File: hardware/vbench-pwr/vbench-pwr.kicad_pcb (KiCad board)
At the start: 2 copper layers, 150 x 136 mm, 39 parts, among them J1 COIL, J10 WAVESHARE-B, J11 WAVESHARE-C, J12 WAVESHARE-D, J2 CHARGE, J3 AUX-BANK, J4 12V-IN, J6 ISENSE, J7 PICO-L, J8 PICO-R, J9 WAVESHARE-A, Q1 IRFP4668, Q2 IRFP4668, Q3 IRFP4668, U1 UCC27524A

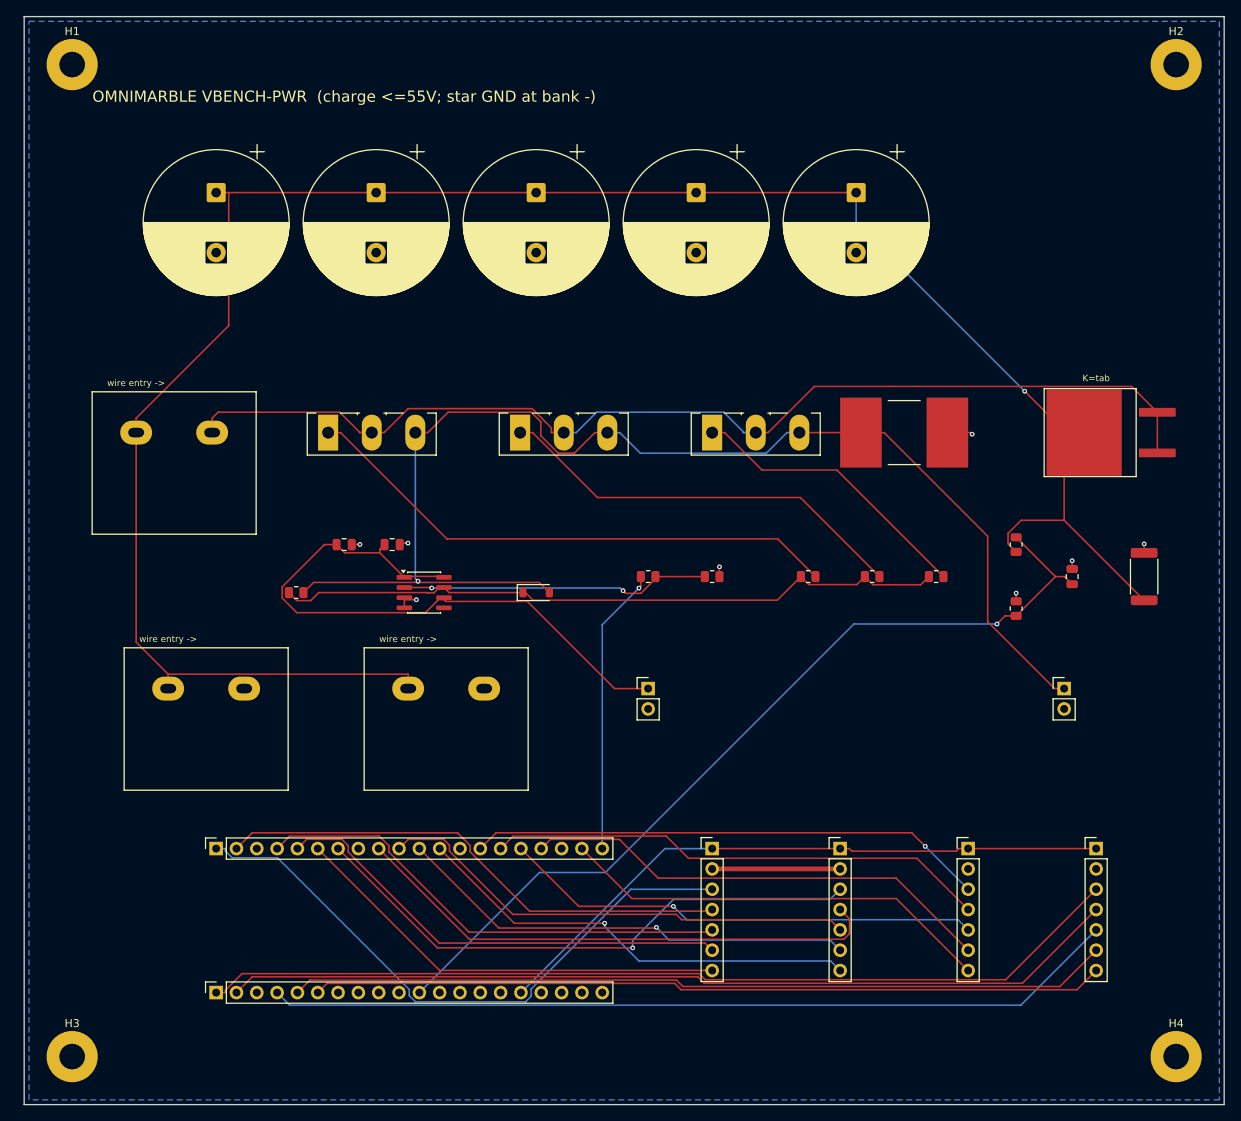
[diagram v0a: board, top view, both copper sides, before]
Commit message: vbench: harden routing to 4-layer with plane-locked inner GND planes
The 2-layer board's B.Cu GND pour fragmented into pockets wherever freerouting
routed a signal across it, and the post-hoc GND stitch was tied to one specific
route (re-routes were non-reproducible). Root cause: a 2-layer board can't hold a
solid GND plane AND route this density on the one remaining signal layer.

Fix = the driver's dedicated-plane pattern, on 4 layers:
- Stackup: F.Cu + B.Cu = signals (2 layers, freerouting completes in ~2s),
  In1 = solid GND plane, In2 = GND plane + a +3V3 pocket over the logic zone.
- plane_lock_dsn() marks In1/In2 (type power) so freerouting never routes a signal
  on them -> the GND plane is never cut, so it can't fragment.
- import drops a GND through-via at each SMD GND pad (freerouting doesn't via them
  down to the inner planes; THT GND pads reach the planes directly).
- +3V3 (all-THT: Pico 3V3 + 4 Waveshare pin-1s) connects through the In2 +3V3
  pocket by via -- no F.Cu/B.Cu routing, so no crossings.

No post-hoc stitching remains. Reproducible: repeated place->route->import runs
give the same DRC-clean board (0 unconnected / 0 parity / 1 cosmetic silk). Back to
4 Waveshare connectors (20 sensor channels). gen_fab: LAYERS_4 + inner 1oz copper.

Co-Authored-By: Claude Opus 4.8 <noreply@anthropic.com>
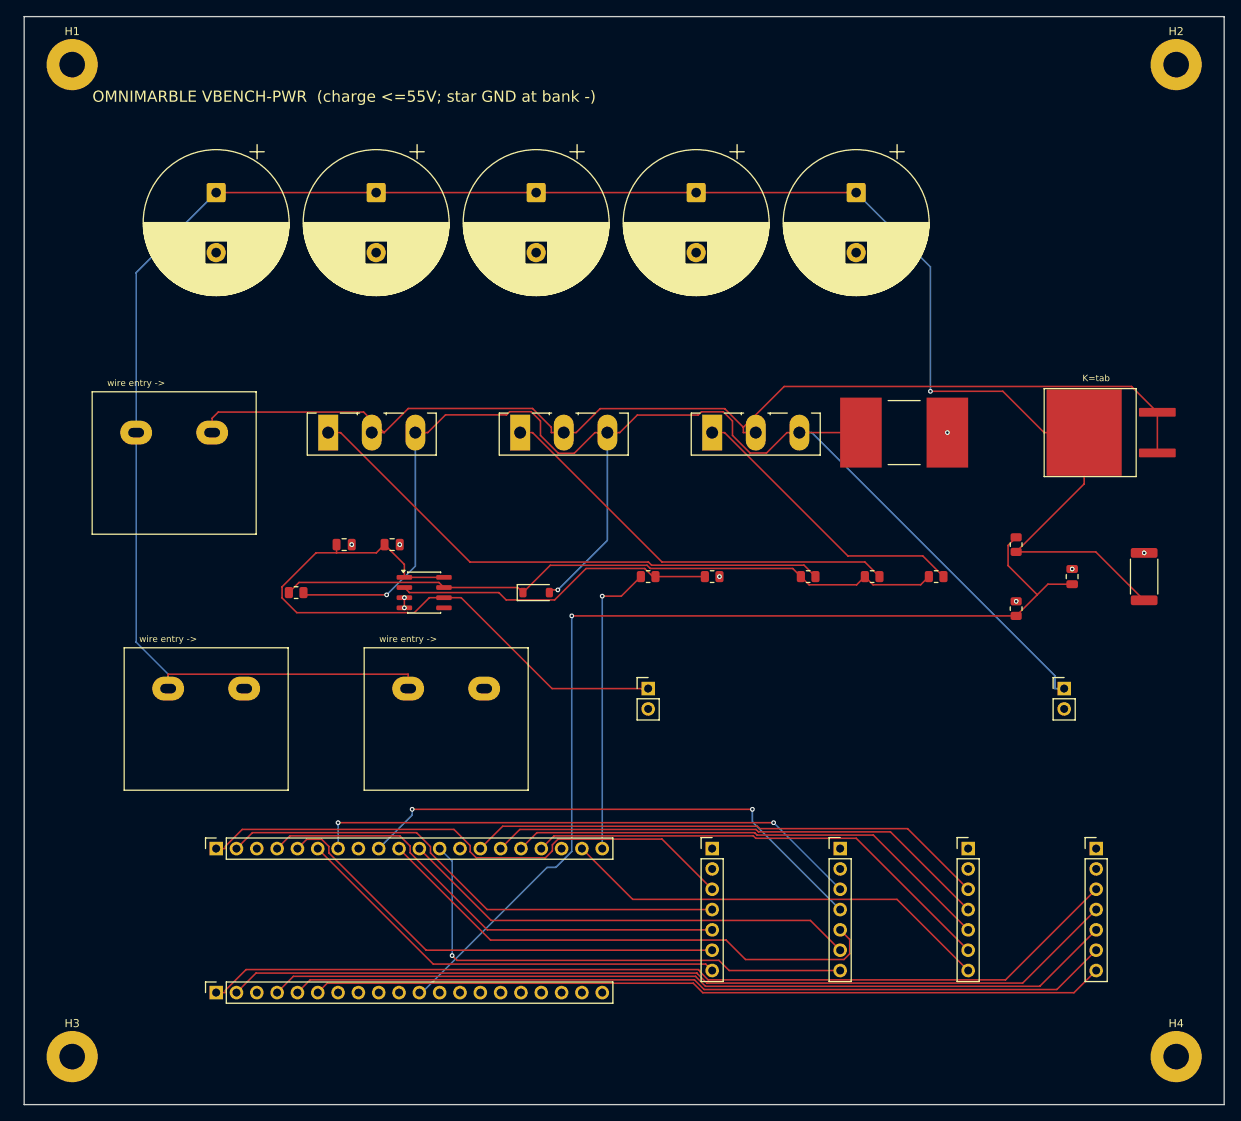
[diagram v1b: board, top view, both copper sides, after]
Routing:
- net +3V3: track 79.6 -> 0.00 mm
- net GND: track 28.5 -> 1.27 mm, vias 8 -> 9
- net VBANK_SENSE: track 110.5 -> 129.1 mm
- net SRC: track 158.7 -> 169.4 mm, vias 1 -> 2
- net VBANK: track 259.1 -> 268.4 mm
- net WA_D0: track 76.9 -> 69.1 mm
- net WB_D4: track 56.6 -> 63.3 mm
- net WB_D2: track 60.7 -> 65.9 mm
- net SW: track 135.2 -> 138.7 mm
- net WB_D0: track 71.5 -> 69.4 mm, vias 1 -> 2
- net WC_D2: track 60.1 -> 61.8 mm, vias 1 -> 0
- net FIRE_IN: track 36.0 -> 37.4 mm
- net FIRE: track 38.9 -> 40.3 mm, vias 2 -> 0
- net WB_D1: track 67.3 -> 66.3 mm, vias 0 -> 2
- net WC_D1: track 62.9 -> 63.6 mm
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- added copper zone on In2.Cu, net +3V3
- added copper zone on In1.Cu, net GND
- added copper zone on In2.Cu, net GND
- removed copper zone on B.Cu, net GND
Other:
- copper layers 2 -> 4
